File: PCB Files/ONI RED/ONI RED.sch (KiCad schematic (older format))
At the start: 8 parts, among them U10 LFE5UM-25F-6BG381C, U2 PCI-Express-4x

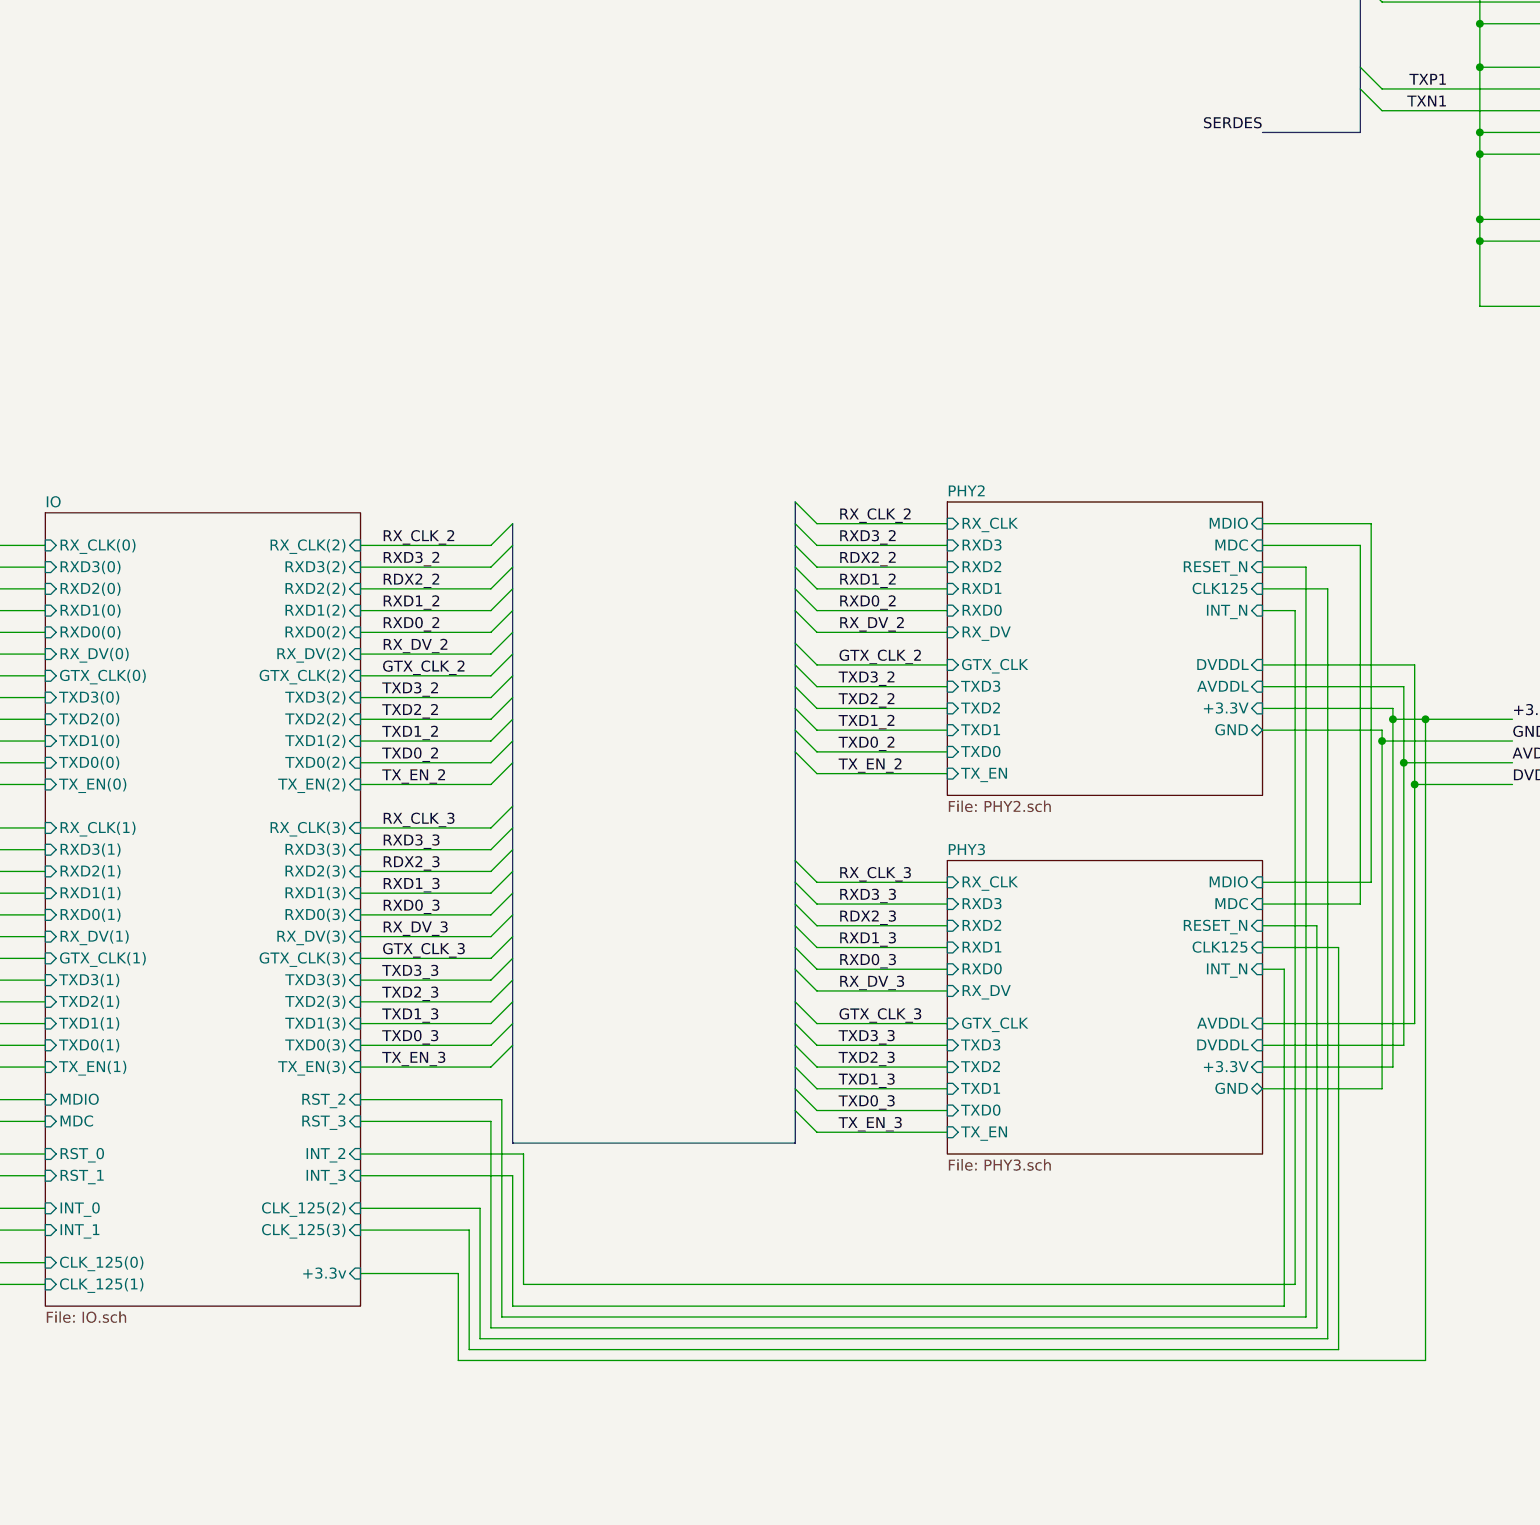
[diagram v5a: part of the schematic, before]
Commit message: Continued routing IO and begun implementing DDR2 RAM
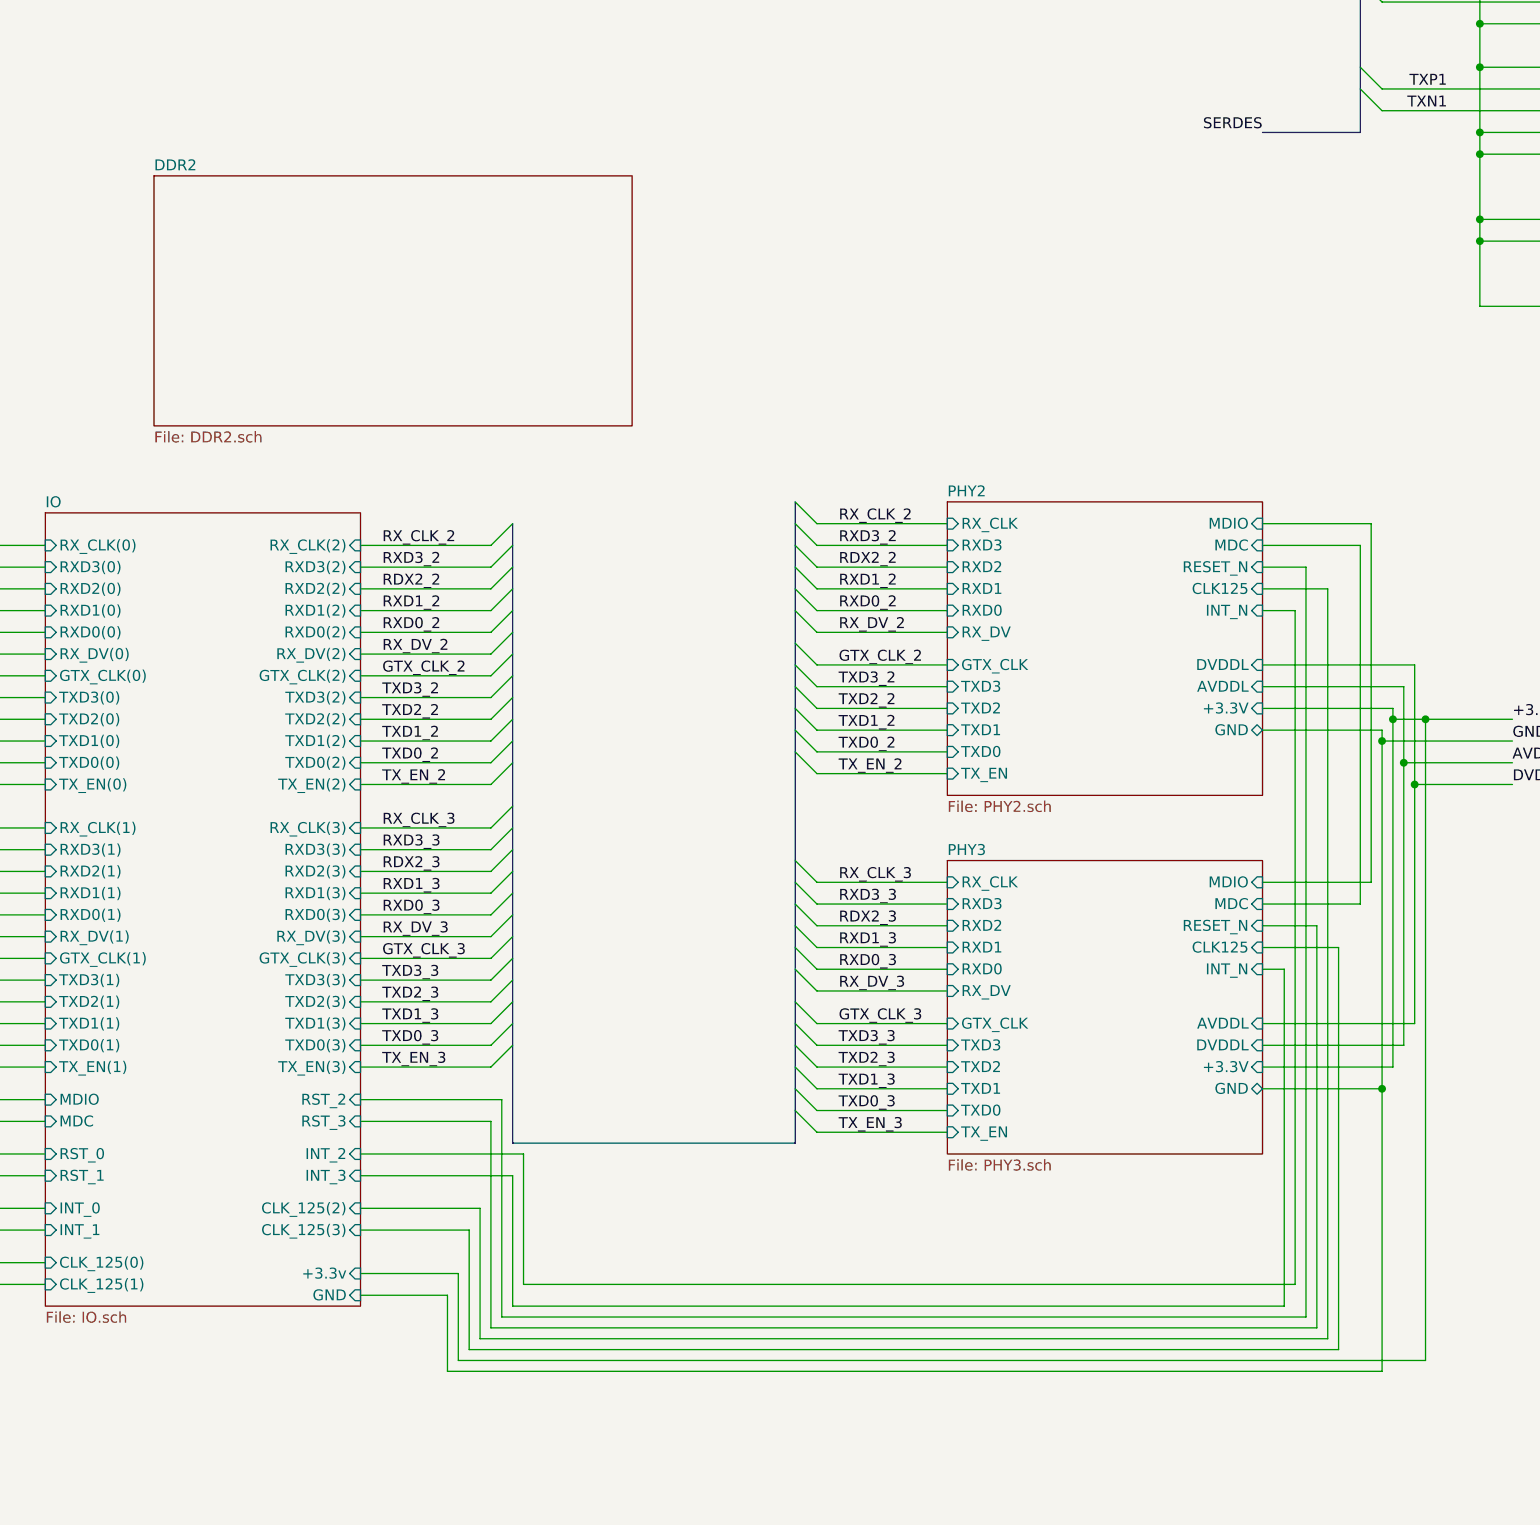
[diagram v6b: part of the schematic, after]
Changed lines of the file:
@@
 $Descr A3 16535 11693
 encoding utf-8
-Sheet 1 8
+Sheet 1 9
 Title ""
 Date ""
@@
 F63 "CLK_125(3)" I R 6450 8250 50
 F64 "CLK_125(2)" I R 6450 8150 50
+F65 "GND" I R 6450 8550 50
 $EndSheet
 Wire Bus Line
@@
 Wire Wire Line
 	11750 6200 11300 6200
+Connection ~ 11300 6200
+Wire Wire Line
+	11300 6200 11300 5650
+Wire Wire Line
+	6450 8550 6850 8550
+Wire Wire Line
+	6850 8550 6850 8900
+Wire Wire Line
+	6850 8900 11150 8900
+Wire Wire Line
+	11150 8900 11150 7600
 Wire Bus Line
 	14600 2200 14600 3000
@@
 Wire Bus Line
 	8450 4900 8450 7850
-Connection ~ 11300 6200
-Wire Wire Line
-	11300 6200 11300 5650
+Connection ~ 11150 7600
+$Sheet
+S 5500 3400 2200 1150
+U 5EE22ECE
+F0 "DDR2" 50
+F1 "DDR2.sch" 50
+$EndSheet
 $EndSCHEMATC

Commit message: Continued DDR work
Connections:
- net FPGA Main/GND: now also C2.2, C3.2, C6.2
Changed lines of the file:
@@
 	4150 1600 4150 950
 Wire Wire Line
-	4150 4250 4150 1600
+	4150 4250 4150 2400
 Connection ~ 4150 1600
 Wire Wire Line
@@
 Wire Wire Line
 	11150 8900 11150 7600
+Connection ~ 11150 7600
+$Sheet
+S 5500 3400 2200 1150
+U 5EE22ECE
+F0 "DDR2" 50
+F1 "DDR2.sch" 50
+$EndSheet
+Wire Wire Line
+	4550 2400 4150 2400
 Wire Bus Line
 	14600 2200 14600 3000
@@
 Wire Bus Line
 	8450 4900 8450 7850
-Connection ~ 11150 7600
-$Sheet
-S 5500 3400 2200 1150
-U 5EE22ECE
-F0 "DDR2" 50
-F1 "DDR2.sch" 50
-$EndSheet
+Connection ~ 4550 2400
+Connection ~ 4150 2400
+Wire Wire Line
+	4150 2400 4150 1600
 $EndSCHEMATC
